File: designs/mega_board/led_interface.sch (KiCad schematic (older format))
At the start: 20 parts

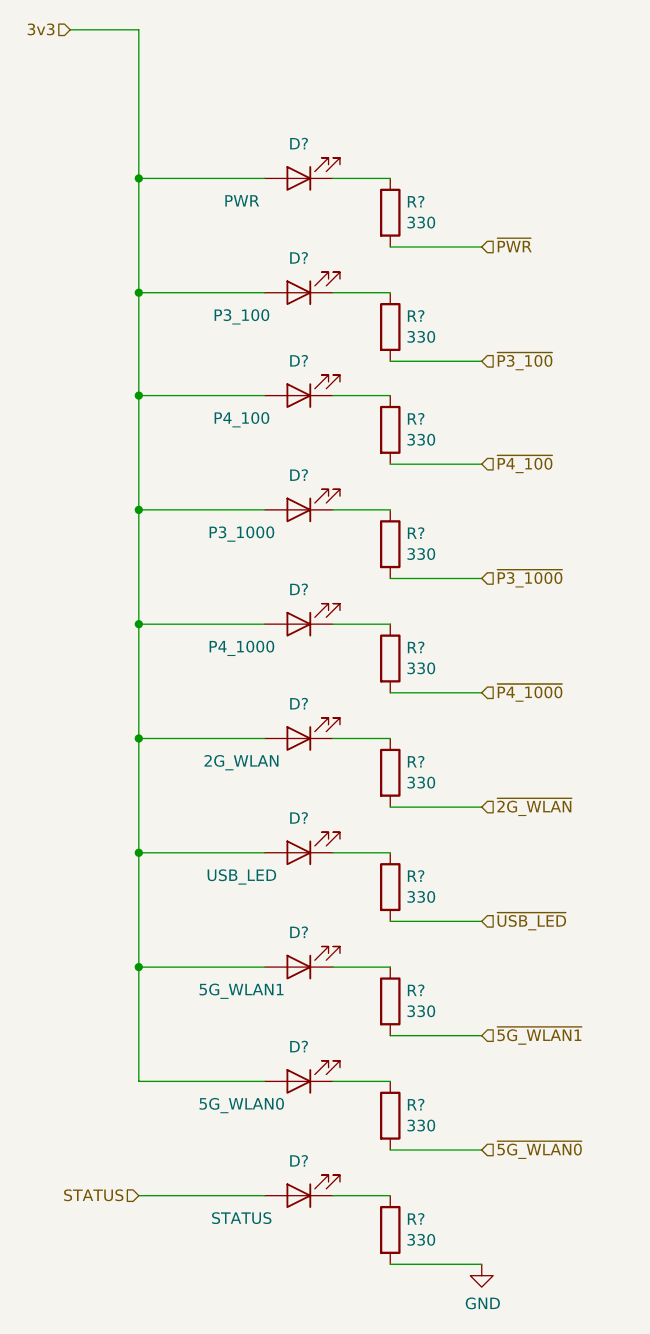
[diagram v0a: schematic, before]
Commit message: Enumerate components as is in eagle design.
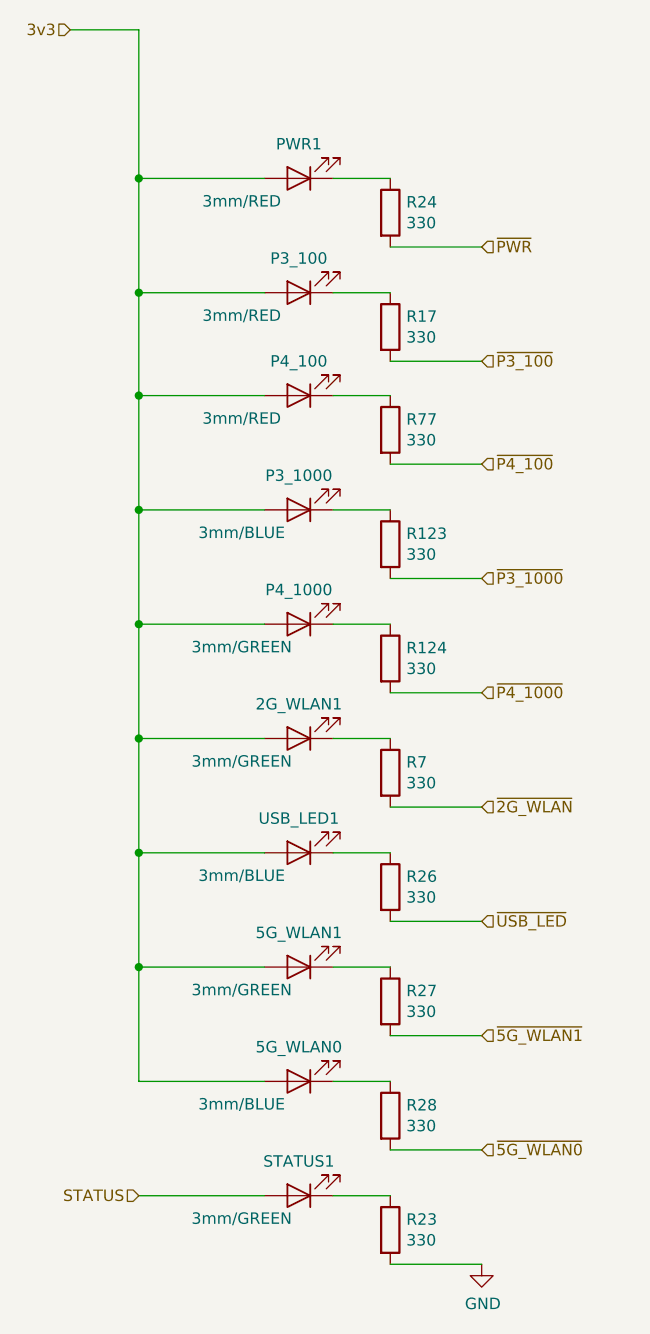
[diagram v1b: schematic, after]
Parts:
- 2G_WLAN1: renamed from D?; value 2G_WLAN -> 3mm/GREEN; footprint (none) -> LibreRouter_MegaBoard:LED3MM
- 5G_WLAN0: renamed from D?; value 5G_WLAN0 -> 3mm/BLUE; footprint (none) -> LibreRouter_MegaBoard:LED3MM
- 5G_WLAN1: renamed from D?; value 5G_WLAN1 -> 3mm/GREEN; footprint (none) -> LibreRouter_MegaBoard:LED3MM
- P3_100: renamed from D?; value P3_100 -> 3mm/RED; footprint (none) -> LibreRouter_MegaBoard:LED3MM
- P3_1000: renamed from D?; value P3_1000 -> 3mm/BLUE; footprint (none) -> LibreRouter_MegaBoard:LED3MM
- P4_100: renamed from D?; value P4_100 -> 3mm/RED; footprint (none) -> LibreRouter_MegaBoard:LED3MM
- P4_1000: renamed from D?; value P4_1000 -> 3mm/GREEN; footprint (none) -> LibreRouter_MegaBoard:LED3MM
- PWR1: renamed from D?; value PWR -> 3mm/RED; footprint (none) -> LibreRouter_MegaBoard:LED3MM
- R123, R124, R17, R23, R24, R26, R27, R28, R7, R77: renamed from R?; footprint (none) -> LibreRouter_MegaBoard:R0402
- STATUS1: renamed from D?; value STATUS -> 3mm/GREEN; footprint (none) -> LibreRouter_MegaBoard:LED3MM
- USB_LED1: renamed from D?; value USB_LED -> 3mm/BLUE; footprint (none) -> LibreRouter_MegaBoard:LED3MM
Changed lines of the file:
@@
 $Descr A4 11693 8268
 encoding utf-8
-Sheet 9 14
+Sheet 14 14
 Title "LibreRouter - Megaboard"
 Date "2019-06-26"
@@
 ~5G_WLAN1
 $Comp
-L Device:R R?
+L Device:R R24
 U 1 1 5D4487F6
 P 5700 1700
-F 0 "R?" H 5770 1746 50  0000 L CNN
+F 0 "R24" H 5770 1746 50  0000 L CNN
 F 1 "330" H 5770 1655 50  0000 L CNN
-F 2 "" V 5630 1700 50  0001 C CNN
+F 2 "LibreRouter_MegaBoard:R0402" V 5630 1700 50  0001 C CNN
 F 3 "~" H 5700 1700 50  0001 C CNN
 	1    5700 1700
@@
 $EndComp
 $Comp
-L Device:LED D?
+L Device:LED PWR1
 U 1 1 5D4489EC
 P 5300 1550
-F 0 "D?" H 5300 1400 50  0000 C CNN
-F 1 "PWR" H 5550 1650 50  0000 C CNN
-F 2 "" H 5300 1550 50  0001 C CNN
+F 0 "PWR1" H 5300 1400 50  0000 C CNN
+F 1 "3mm/RED" H 5550 1650 50  0000 C CNN
+F 2 "LibreRouter_MegaBoard:LED3MM" H 5300 1550 50  0001 C CNN
 F 3 "~" H 5300 1550 50  0001 C CNN
 	1    5300 1550
@@
 	5700 1850 6100 1850
 $Comp
-L Device:R R?
+L Device:R R17
 U 1 1 5D449CFE
 P 5700 2200
-F 0 "R?" H 5770 2246 50  0000 L CNN
+F 0 "R17" H 5770 2246 50  0000 L CNN
 F 1 "330" H 5770 2155 50  0000 L CNN
-F 2 "" V 5630 2200 50  0001 C CNN
+F 2 "LibreRouter_MegaBoard:R0402" V 5630 2200 50  0001 C CNN
 F 3 "~" H 5700 2200 50  0001 C CNN
 	1    5700 2200
@@
 $EndComp
 $Comp
-L Device:LED D?
+L Device:LED P3_100
 U 1 1 5D449D05
 P 5300 2050
-F 0 "D?" H 5300 1900 50  0000 C CNN
-F 1 "P3_100" H 5550 2150 50  0000 C CNN
-F 2 "" H 5300 2050 50  0001 C CNN
+F 0 "P3_100" H 5300 1900 50  0000 C CNN
+F 1 "3mm/RED" H 5550 2150 50  0000 C CNN
+F 2 "LibreRouter_MegaBoard:LED3MM" H 5300 2050 50  0001 C CNN
 F 3 "~" H 5300 2050 50  0001 C CNN
 	1    5300 2050
@@
 	5700 2350 6100 2350
 $Comp
-L Device:R R?
+L Device:R R77
 U 1 1 5D449EF1
 P 5700 2650
-F 0 "R?" H 5770 2696 50  0000 L CNN
+F 0 "R77" H 5770 2696 50  0000 L CNN
 F 1 "330" H 5770 2605 50  0000 L CNN
-F 2 "" V 5630 2650 50  0001 C CNN
+F 2 "LibreRouter_MegaBoard:R0402" V 5630 2650 50  0001 C CNN
 F 3 "~" H 5700 2650 50  0001 C CNN
 	1    5700 2650
@@
 $EndComp
 $Comp
-L Device:LED D?
+L Device:LED P4_100
 U 1 1 5D449EF8
 P 5300 2500
-F 0 "D?" H 5300 2350 50  0000 C CNN
-F 1 "P4_100" H 5550 2600 50  0000 C CNN
-F 2 "" H 5300 2500 50  0001 C CNN
+F 0 "P4_100" H 5300 2350 50  0000 C CNN
+F 1 "3mm/RED" H 5550 2600 50  0000 C CNN
+F 2 "LibreRouter_MegaBoard:LED3MM" H 5300 2500 50  0001 C CNN
 F 3 "~" H 5300 2500 50  0001 C CNN
 	1    5300 2500
@@
 	5700 2800 6100 2800
 $Comp
-L Device:R R?
+L Device:R R123
 U 1 1 5D449F02
 P 5700 3150
-F 0 "R?" H 5770 3196 50  0000 L CNN
+F 0 "R123" H 5770 3196 50  0000 L CNN
 F 1 "330" H 5770 3105 50  0000 L CNN
-F 2 "" V 5630 3150 50  0001 C CNN
+F 2 "LibreRouter_MegaBoard:R0402" V 5630 3150 50  0001 C CNN
 F 3 "~" H 5700 3150 50  0001 C CNN
 	1    5700 3150
@@
 $EndComp
 $Comp
-L Device:LED D?
+L Device:LED P3_1000
 U 1 1 5D449F09
 P 5300 3000
-F 0 "D?" H 5300 2850 50  0000 C CNN
-F 1 "P3_1000" H 5550 3100 50  0000 C CNN
-F 2 "" H 5300 3000 50  0001 C CNN
+F 0 "P3_1000" H 5300 2850 50  0000 C CNN
+F 1 "3mm/BLUE" H 5550 3100 50  0000 C CNN
+F 2 "LibreRouter_MegaBoard:LED3MM" H 5300 3000 50  0001 C CNN
 F 3 "~" H 5300 3000 50  0001 C CNN
 	1    5300 3000
@@
 	5700 3300 6100 3300
 $Comp
-L Device:R R?
+L Device:R R124
 U 1 1 5D44A5F7
 P 5700 3650
-F 0 "R?" H 5770 3696 50  0000 L CNN
+F 0 "R124" H 5770 3696 50  0000 L CNN
 F 1 "330" H 5770 3605 50  0000 L CNN
-F 2 "" V 5630 3650 50  0001 C CNN
+F 2 "LibreRouter_MegaBoard:R0402" V 5630 3650 50  0001 C CNN
 F 3 "~" H 5700 3650 50  0001 C CNN
 	1    5700 3650
@@
 $EndComp
 $Comp
-L Device:LED D?
+L Device:LED P4_1000
 U 1 1 5D44A5FE
 P 5300 3500
-F 0 "D?" H 5300 3350 50  0000 C CNN
-F 1 "P4_1000" H 5550 3600 50  0000 C CNN
-F 2 "" H 5300 3500 50  0001 C CNN
+F 0 "P4_1000" H 5300 3350 50  0000 C CNN
+F 1 "3mm/GREEN" H 5550 3600 50  0000 C CNN
+F 2 "LibreRouter_MegaBoard:LED3MM" H 5300 3500 50  0001 C CNN
 F 3 "~" H 5300 3500 50  0001 C CNN
 	1    5300 3500
@@
 	5700 3800 6100 3800
 $Comp
-L Device:R R?
+L Device:R R7
 U 1 1 5D44A608
 P 5700 4150
-F 0 "R?" H 5770 4196 50  0000 L CNN
+F 0 "R7" H 5770 4196 50  0000 L CNN
 F 1 "330" H 5770 4105 50  0000 L CNN
-F 2 "" V 5630 4150 50  0001 C CNN
+F 2 "LibreRouter_MegaBoard:R0402" V 5630 4150 50  0001 C CNN
 F 3 "~" H 5700 4150 50  0001 C CNN
 	1    5700 4150
@@
 $EndComp
 $Comp
-L Device:LED D?
+L Device:LED 2G_WLAN1
 U 1 1 5D44A60F
 P 5300 4000
-F 0 "D?" H 5300 3850 50  0000 C CNN
-F 1 "2G_WLAN" H 5550 4100 50  0000 C CNN
-F 2 "" H 5300 4000 50  0001 C CNN
+F 0 "2G_WLAN1" H 5300 3850 50  0000 C CNN
+F 1 "3mm/GREEN" H 5550 4100 50  0000 C CNN
+F 2 "LibreRouter_MegaBoard:LED3MM" H 5300 4000 50  0001 C CNN
 F 3 "~" H 5300 4000 50  0001 C CNN
 	1    5300 4000
@@
 	5700 4300 6100 4300
 $Comp
-L Device:R R?
+L Device:R R26
 U 1 1 5D44A619
 P 5700 4650
-F 0 "R?" H 5770 4696 50  0000 L CNN
+F 0 "R26" H 5770 4696 50  0000 L CNN
 F 1 "330" H 5770 4605 50  0000 L CNN
-F 2 "" V 5630 4650 50  0001 C CNN
+F 2 "LibreRouter_MegaBoard:R0402" V 5630 4650 50  0001 C CNN
 F 3 "~" H 5700 4650 50  0001 C CNN
 	1    5700 4650
@@
 $EndComp
 $Comp
-L Device:LED D?
+L Device:LED USB_LED1
 U 1 1 5D44A620
 P 5300 4500
-F 0 "D?" H 5300 4350 50  0000 C CNN
-F 1 "USB_LED" H 5550 4600 50  0000 C CNN
-F 2 "" H 5300 4500 50  0001 C CNN
+F 0 "USB_LED1" H 5300 4350 50  0000 C CNN
+F 1 "3mm/BLUE" H 5550 4600 50  0000 C CNN
+F 2 "LibreRouter_MegaBoard:LED3MM" H 5300 4500 50  0001 C CNN
 F 3 "~" H 5300 4500 50  0001 C CNN
 	1    5300 4500
@@
 	5700 4800 6100 4800
 $Comp
-L Device:R R?
+L Device:R R27
 U 1 1 5D44A62A
 P 5700 5150
-F 0 "R?" H 5770 5196 50  0000 L CNN
+F 0 "R27" H 5770 5196 50  0000 L CNN
 F 1 "330" H 5770 5105 50  0000 L CNN
-F 2 "" V 5630 5150 50  0001 C CNN
+F 2 "LibreRouter_MegaBoard:R0402" V 5630 5150 50  0001 C CNN
 F 3 "~" H 5700 5150 50  0001 C CNN
 	1    5700 5150
@@
 $EndComp
 $Comp
-L Device:LED D?
+L Device:LED 5G_WLAN1
 U 1 1 5D44A631
 P 5300 5000
-F 0 "D?" H 5300 4850 50  0000 C CNN
-F 1 "5G_WLAN1" H 5550 5100 50  0000 C CNN
-F 2 "" H 5300 5000 50  0001 C CNN
+F 0 "5G_WLAN1" H 5300 4850 50  0000 C CNN
+F 1 "3mm/GREEN" H 5550 5100 50  0000 C CNN
+F 2 "LibreRouter_MegaBoard:LED3MM" H 5300 5000 50  0001 C CNN
 F 3 "~" H 5300 5000 50  0001 C CNN
 	1    5300 5000
@@
 	4600 3500 4600 4000
 $Comp
-L Device:R R?
+L Device:R R28
 U 1 1 5D44B71E
 P 5700 5650
-F 0 "R?" H 5770 5696 50  0000 L CNN
+F 0 "R28" H 5770 5696 50  0000 L CNN
 F 1 "330" H 5770 5605 50  0000 L CNN
-F 2 "" V 5630 5650 50  0001 C CNN
+F 2 "LibreRouter_MegaBoard:R0402" V 5630 5650 50  0001 C CNN
 F 3 "~" H 5700 5650 50  0001 C CNN
 	1    5700 5650
@@
 $EndComp
 $Comp
-L Device:LED D?
+L Device:LED 5G_WLAN0
 U 1 1 5D44B725
 P 5300 5500
-F 0 "D?" H 5300 5350 50  0000 C CNN
-F 1 "5G_WLAN0" H 5550 5600 50  0000 C CNN
-F 2 "" H 5300 5500 50  0001 C CNN
+F 0 "5G_WLAN0" H 5300 5350 50  0000 C CNN
+F 1 "3mm/BLUE" H 5550 5600 50  0000 C CNN
+F 2 "LibreRouter_MegaBoard:LED3MM" H 5300 5500 50  0001 C CNN
 F 3 "~" H 5300 5500 50  0001 C CNN
 	1    5300 5500
@@
 	5700 5800 6100 5800
 $Comp
-L Device:R R?
+L Device:R R23
 U 1 1 5D44BE47
 P 5700 6150
-F 0 "R?" H 5770 6196 50  0000 L CNN
+F 0 "R23" H 5770 6196 50  0000 L CNN
 F 1 "330" H 5770 6105 50  0000 L CNN
-F 2 "" V 5630 6150 50  0001 C CNN
+F 2 "LibreRouter_MegaBoard:R0402" V 5630 6150 50  0001 C CNN
 F 3 "~" H 5700 6150 50  0001 C CNN
 	1    5700 6150
@@
 $EndComp
 $Comp
-L Device:LED D?
+L Device:LED STATUS1
 U 1 1 5D44BE4E
 P 5300 6000
-F 0 "D?" H 5300 5850 50  0000 C CNN
-F 1 "STATUS" H 5550 6100 50  0000 C CNN
-F 2 "" H 5300 6000 50  0001 C CNN
+F 0 "STATUS1" H 5300 5850 50  0000 C CNN
+F 1 "3mm/GREEN" H 5550 6100 50  0000 C CNN
+F 2 "LibreRouter_MegaBoard:LED3MM" H 5300 6000 50  0001 C CNN
 F 3 "~" H 5300 6000 50  0001 C CNN
 	1    5300 6000
@@
 Connection ~ 4600 5000
 $Comp
-L power:GND #PWR?
+L power:GND #PWR0194
 U 1 1 5D44E78E
 P 6100 6300
-F 0 "#PWR?" H 6100 6050 50  0001 C CNN
+F 0 "#PWR0194" H 6100 6050 50  0001 C CNN
 F 1 "GND" H 6105 6127 50  0000 C CNN
 F 2 "" H 6100 6300 50  0001 C CNN

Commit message: Add BOM definition to all resistors
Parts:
- R123, R124, R17, R23, R24, R26, R27, R28, R7, R77: Manufacturer (none) -> Panasonic Electronic Components; Manufacturer PN (none) -> ERJ-PA2F3300X; Supplier (none) -> DigiKey; Supplier PN (none) -> P17221DKR-ND
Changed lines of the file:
@@
 F 2 "LibreRouter_MegaBoard:R0402" V 5630 1700 50  0001 C CNN
 F 3 "~" H 5700 1700 50  0001 C CNN
+F 4 "Panasonic Electronic Components" H 5700 1700 50  0001 C CNN "Manufacturer"
+F 5 "ERJ-PA2F3300X" H 5700 1700 50  0001 C CNN "Manufacturer PN"
+F 6 "DigiKey" H 5700 1700 50  0001 C CNN "Supplier"
+F 7 "P17221DKR-ND" H 5700 1700 50  0001 C CNN "Supplier PN"
 	1    5700 1700
 	1    0    0    -1
@@
 F 2 "LibreRouter_MegaBoard:R0402" V 5630 2200 50  0001 C CNN
 F 3 "~" H 5700 2200 50  0001 C CNN
+F 4 "Panasonic Electronic Components" H 5700 2200 50  0001 C CNN "Manufacturer"
+F 5 "ERJ-PA2F3300X" H 5700 2200 50  0001 C CNN "Manufacturer PN"
+F 6 "DigiKey" H 5700 2200 50  0001 C CNN "Supplier"
+F 7 "P17221DKR-ND" H 5700 2200 50  0001 C CNN "Supplier PN"
 	1    5700 2200
 	1    0    0    -1
@@
 F 2 "LibreRouter_MegaBoard:R0402" V 5630 2650 50  0001 C CNN
 F 3 "~" H 5700 2650 50  0001 C CNN
+F 4 "Panasonic Electronic Components" H 5700 2650 50  0001 C CNN "Manufacturer"
+F 5 "ERJ-PA2F3300X" H 5700 2650 50  0001 C CNN "Manufacturer PN"
+F 6 "DigiKey" H 5700 2650 50  0001 C CNN "Supplier"
+F 7 "P17221DKR-ND" H 5700 2650 50  0001 C CNN "Supplier PN"
 	1    5700 2650
 	1    0    0    -1
@@
 F 2 "LibreRouter_MegaBoard:R0402" V 5630 3150 50  0001 C CNN
 F 3 "~" H 5700 3150 50  0001 C CNN
+F 4 "Panasonic Electronic Components" H 5700 3150 50  0001 C CNN "Manufacturer"
+F 5 "ERJ-PA2F3300X" H 5700 3150 50  0001 C CNN "Manufacturer PN"
+F 6 "DigiKey" H 5700 3150 50  0001 C CNN "Supplier"
+F 7 "P17221DKR-ND" H 5700 3150 50  0001 C CNN "Supplier PN"
 	1    5700 3150
 	1    0    0    -1
@@
 F 2 "LibreRouter_MegaBoard:R0402" V 5630 3650 50  0001 C CNN
 F 3 "~" H 5700 3650 50  0001 C CNN
+F 4 "Panasonic Electronic Components" H 5700 3650 50  0001 C CNN "Manufacturer"
+F 5 "ERJ-PA2F3300X" H 5700 3650 50  0001 C CNN "Manufacturer PN"
+F 6 "DigiKey" H 5700 3650 50  0001 C CNN "Supplier"
+F 7 "P17221DKR-ND" H 5700 3650 50  0001 C CNN "Supplier PN"
 	1    5700 3650
 	1    0    0    -1
@@
 F 2 "LibreRouter_MegaBoard:R0402" V 5630 4150 50  0001 C CNN
 F 3 "~" H 5700 4150 50  0001 C CNN
+F 4 "Panasonic Electronic Components" H 5700 4150 50  0001 C CNN "Manufacturer"
+F 5 "ERJ-PA2F3300X" H 5700 4150 50  0001 C CNN "Manufacturer PN"
+F 6 "DigiKey" H 5700 4150 50  0001 C CNN "Supplier"
+F 7 "P17221DKR-ND" H 5700 4150 50  0001 C CNN "Supplier PN"
 	1    5700 4150
 	1    0    0    -1
@@
 F 2 "LibreRouter_MegaBoard:R0402" V 5630 4650 50  0001 C CNN
 F 3 "~" H 5700 4650 50  0001 C CNN
+F 4 "Panasonic Electronic Components" H 5700 4650 50  0001 C CNN "Manufacturer"
+F 5 "ERJ-PA2F3300X" H 5700 4650 50  0001 C CNN "Manufacturer PN"
+F 6 "DigiKey" H 5700 4650 50  0001 C CNN "Supplier"
+F 7 "P17221DKR-ND" H 5700 4650 50  0001 C CNN "Supplier PN"
 	1    5700 4650
 	1    0    0    -1
@@
 F 2 "LibreRouter_MegaBoard:R0402" V 5630 5150 50  0001 C CNN
 F 3 "~" H 5700 5150 50  0001 C CNN
+F 4 "Panasonic Electronic Components" H 5700 5150 50  0001 C CNN "Manufacturer"
+F 5 "ERJ-PA2F3300X" H 5700 5150 50  0001 C CNN "Manufacturer PN"
+F 6 "DigiKey" H 5700 5150 50  0001 C CNN "Supplier"
+F 7 "P17221DKR-ND" H 5700 5150 50  0001 C CNN "Supplier PN"
 	1    5700 5150
 	1    0    0    -1
@@
 F 2 "LibreRouter_MegaBoard:R0402" V 5630 5650 50  0001 C CNN
 F 3 "~" H 5700 5650 50  0001 C CNN
+F 4 "Panasonic Electronic Components" H 5700 5650 50  0001 C CNN "Manufacturer"
+F 5 "ERJ-PA2F3300X" H 5700 5650 50  0001 C CNN "Manufacturer PN"
+F 6 "DigiKey" H 5700 5650 50  0001 C CNN "Supplier"
+F 7 "P17221DKR-ND" H 5700 5650 50  0001 C CNN "Supplier PN"
 	1    5700 5650
 	1    0    0    -1
@@
 F 2 "LibreRouter_MegaBoard:R0402" V 5630 6150 50  0001 C CNN
 F 3 "~" H 5700 6150 50  0001 C CNN
+F 4 "Panasonic Electronic Components" H 5700 6150 50  0001 C CNN "Manufacturer"
+F 5 "ERJ-PA2F3300X" H 5700 6150 50  0001 C CNN "Manufacturer PN"
+F 6 "DigiKey" H 5700 6150 50  0001 C CNN "Supplier"
+F 7 "P17221DKR-ND" H 5700 6150 50  0001 C CNN "Supplier PN"
 	1    5700 6150
 	1    0    0    -1
